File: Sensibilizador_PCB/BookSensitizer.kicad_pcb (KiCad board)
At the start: 2 copper layers, 100 x 100 mm, 37 parts, among them J1 Jack_out, J2 Jack_in, J3 Conn_inputs, M1 Fan, Q1 IRF630, Q2 IRF630, Q3 IRF630, Q4 IRF630, Q5 SI2302, U1 LM5104M, U2 LM5104M

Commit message: Organizado 0 aire
0 aire
ready pa rutear
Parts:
- added REF**: MountingHole_2.5mm, MountingHole:MountingHole_2.5mm, F.Cu at (113.1, 88.9)
- added REF**: MountingHole_2.5mm, MountingHole:MountingHole_2.5mm, F.Cu at (175.0, 123.5)
- added REF**: MountingHole_2.5mm, MountingHole:MountingHole_2.5mm, F.Cu at (113.6, 122.9)
- J1 Vout: renamed from J1
- J2 Vin: renamed from J2
- moved D7 69.9 mm to (166.6, 92.8), turned to -90 degrees
- moved L1 67.8 mm to (136.7, 123.9)
- moved D6 65.5 mm to (121.6, 90.9), turned to 90 degrees
- moved D8 62.5 mm to (166.6, 116.4), turned to 90 degrees
- moved D5 58.8 mm to (121.6, 114.7), turned to 90 degrees
- moved M1 33.2 mm to (176.3, 90.3), turned to 90 degrees
- moved U1 27.4 mm to (119.9, 103.6), turned to 90 degrees
- moved C6 24.9 mm to (167.4, 99.0), turned to 180 degrees
- moved R2 24.6 mm to (119.1, 114.8), turned to -90 degrees
- moved Q5 24.5 mm to (170.4, 86.1), turned to 0 degrees
- moved R7 23.8 mm to (169.1, 116.4), turned to -90 degrees
- moved Q2 23.3 mm to (125.0, 89.3), turned to -90 degrees
- moved D2 22.9 mm to (135.9, 89.3), turned to -90 degrees
- moved J1 Vout 22.7 mm to (164.9, 78.9), turned to 180 degrees
- moved R3 22.0 mm to (120.2, 94.8)
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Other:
- board size 100 x 100 mm -> 70 x 57 mm
- board text added: "+"
- board text added: "-"
- board text added: "Fan"
- board text added: "GND"
- board text added: "PWM1"
- board text added: "PWM2"

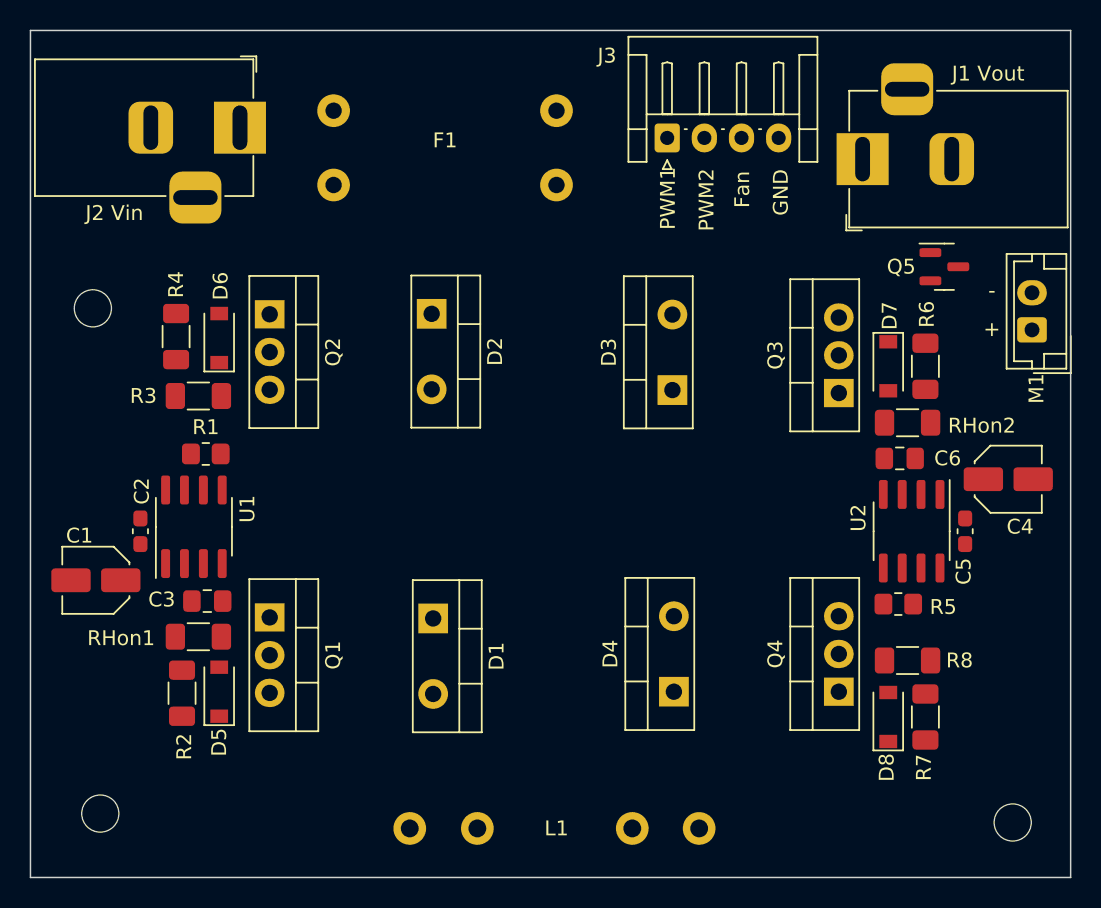
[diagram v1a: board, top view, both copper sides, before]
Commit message: mini cambio en label de RHon
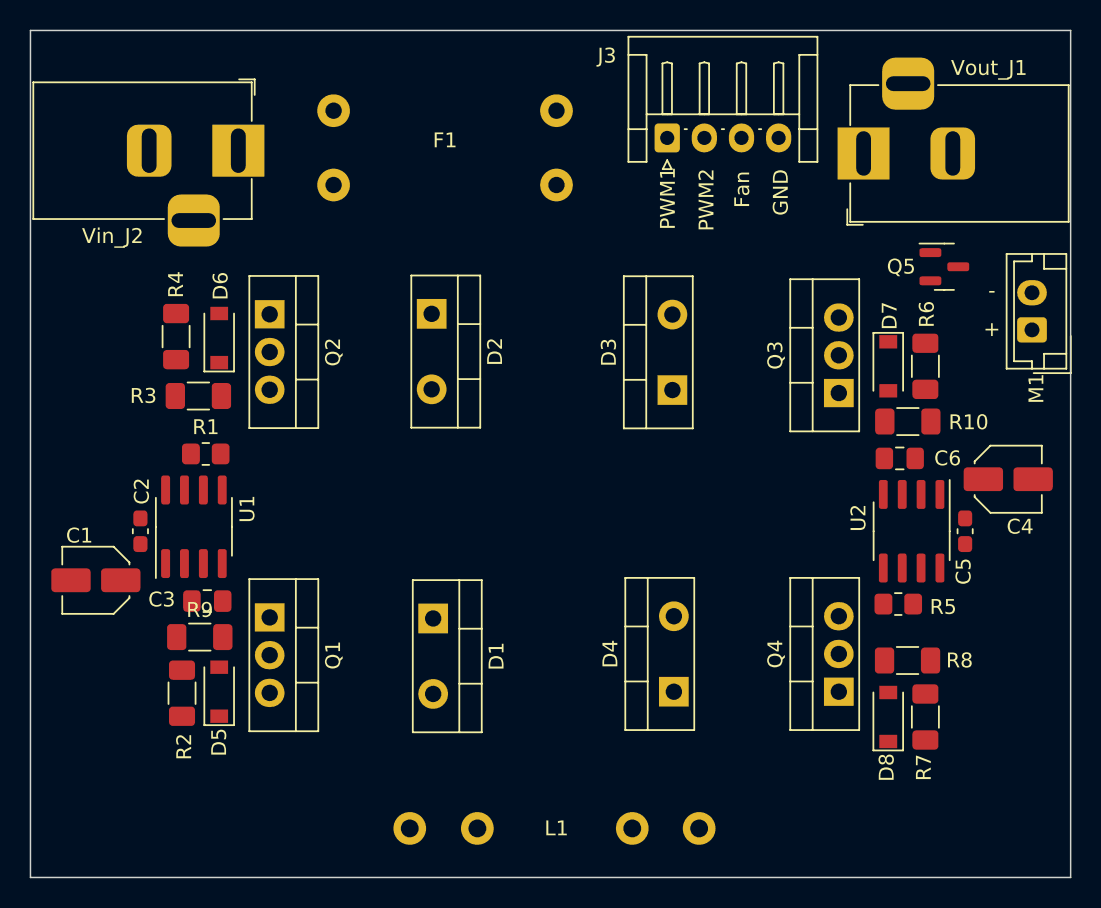
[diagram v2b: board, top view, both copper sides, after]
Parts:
- removed J1 Vout: Jack_out, Connector_BarrelJack:BarrelJack_Horizontal
- removed J2 Vin: Jack_in, Connector_BarrelJack:BarrelJack_Horizontal
- removed REF** (x3): MountingHole_2.5mm, MountingHole:MountingHole_2.5mm
- removed RHon1, RHon2: 2.74 1/4W, Resistor_SMD:R_1206_3216Metric_Pad1.30x1.75mm_HandSolder
- added R10: 2.74 1/4W, Resistor_SMD:R_1206_3216Metric_Pad1.30x1.75mm_HandSolder, F.Cu at (167.9, 96.5)
- added R9: 2.74 1/4W, Resistor_SMD:R_1206_3216Metric_Pad1.30x1.75mm_HandSolder, F.Cu at (120.3, 111.0)
- added Vin_J2: Jack_in, Connector_BarrelJack:BarrelJack_Horizontal, F.Cu at (122.9, 78.3)
- added Vout_J1: Jack_out, Connector_BarrelJack:BarrelJack_Horizontal, F.Cu at (165.0, 78.5)

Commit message: la mitad de los trazos
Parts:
- moved C3 7.00 mm to (124.7, 102.8)
- moved C6 5.71 mm to (163.3, 103.0)
- moved D5 3.63 mm to (121.6, 111.1)
- moved R2 3.63 mm to (119.1, 111.2)
- moved R9 3.63 mm to (120.3, 107.4)
- moved C1 1.57 mm to (113.4, 105.6)
- moved C2 1.57 mm to (116.4, 102.3)
- moved R1 1.57 mm to (120.8, 97.1)
- moved U1 1.57 mm to (120.0, 102.0)
- moved R5 0.55 mm to (167.3, 108.3)
- moved U2 0.47 mm to (168.1, 103.4)
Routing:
- net /in_1: track 0.00 -> 55.5 mm, vias 0 -> 2
- net /in_2: track 0.00 -> 43.6 mm, vias 0 -> 2
- net /in_3: track 0.00 -> 19.1 mm
- net Net-(R7-Pad1): track 0.00 -> 9.33 mm
- net Net-(R6-Pad1): track 0.00 -> 8.34 mm
- net Net-(R3-Pad1): track 0.00 -> 7.40 mm
- net Net-(R2-Pad1): track 0.00 -> 6.60 mm
- net Net-(M1-Pad2): track 0.00 -> 6.35 mm
- net /driver1/G_low: track 0.00 -> 6.32 mm
- net Net-(C6-Pad1): track 0.00 -> 6.24 mm
- net Net-(C3-Pad1): track 0.00 -> 5.75 mm
- net /driver2/Hs: track 0.00 -> 5.73 mm
- net /driver1/G_High: track 0.00 -> 5.62 mm
- net /driver2/G_low: track 0.00 -> 5.60 mm
- net /driver2/G_High: track 0.00 -> 5.55 mm
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- added copper zone on B.Cu, net /driver1/Hs

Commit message: PCB lista
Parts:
- moved Q5 0.87 mm to (171.3, 86.1)
- moved M1 0.19 mm to (176.1, 90.3)
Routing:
- net Net-(F1-Pad1): track 0.00 -> 19.9 mm
- net +12V: track 0.00 -> 6.05 mm
- net GND: track 0.00 -> 5.16 mm
- net Net-(M1-Pad2): track 6.35 -> 5.39 mm
- net /in_3: track 19.1 -> 19.4 mm, vias 0 -> 1
- net /in_1: track 55.5 -> 55.4 mm, vias 2 -> 1
- net /in_2: vias 2 -> 1
- net /driver2/Hs: vias 0 -> 1
- net /driver1/Hs: vias 0 -> 1
- added copper zone on F.Cu, net +12V
- added copper zone on B.Cu, net /driver2/Hs
- added copper zone on F.Cu, net GND

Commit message: Con tornillos
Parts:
- added T1: MountingHole_3.2mm_M3, MountingHole:MountingHole_3.2mm_M3, F.Cu at (115.4, 120.4)
- added T2: MountingHole_3.2mm_M3, MountingHole:MountingHole_3.2mm_M3, F.Cu at (113.9, 87.8)
- added T3: MountingHole_3.2mm_M3, MountingHole:MountingHole_3.2mm_M3, F.Cu at (173.2, 121.9)
- F1 10A: renamed from F1
- moved C2 0.55 mm to (116.4, 101.8)
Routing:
- net +12V: track 6.05 -> 0.03 mm
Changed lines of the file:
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@@
   )
   (footprint "Capacitor_SMD:C_0603_1608Metric_Pad1.08x0.95mm_HandSolder" (layer "F.Cu")
-    (at 116.3714 102.3326 90)
+    (at 116.3828 101.7778 90)
     (descr "Capacitor SMD 0603 (1608 Metric), square (rectangular) end terminal, IPC_7351 nominal with elongated pad for handsoldering. (Body size source: IPC-SM-782 page 76, https://www.pcb-3d.com/wordpress/wp-content/uploads/ipc-sm-782a_amendment_1_and_2.pdf), generated with kicad-footprint-generator")
     (tags "capacitor handsolder")
@@
     (property "Sheetname" "")
     (attr through_hole)
-    (fp_text reference "Vin_J2" (at -8.45 5.75) (layer "F.SilkS")
+    (fp_text reference "Vin_J2" (at -8.5908 -5.6973) (layer "F.SilkS")
       (effects (font (size 1 1) (thickness 0.15)))
     )
@@
     )
   )
+  (footprint "MountingHole:MountingHole_3.2mm_M3" (layer "F.Cu")
+    (at 113.9444 87.8332)
+    (descr "Mounting Hole 3.2mm, no annular, M3")
+    (tags "mounting hole 3.2mm no annular m3")
+    (attr exclude_from_pos_files exclude_from_bom)
+    (fp_text reference "T2" (at 0 -4.2) (layer "User.1")
+      (effects (font (size 1 1) (thickness 0.15)))
+    )
+    (fp_text value "MountingHole_3.2mm_M3" (at 0 4.2) (layer "F.Fab")
+      (effects (font (size 1 1) (thickness 0.15)))
+    )
+    (fp_text user "${REFERENCE}" (at 0 0) (layer "F.Fab")
+      (effects (font (size 1 1) (thickness 0.15)))
+    )
+    (fp_circle (center 0 0) (end 3.2 0) (layer "Cmts.User") (width 0.15) (fill none))
+    (fp_circle (center 0 0) (end 3.45 0) (layer "F.CrtYd") (width 0.05) (fill none))
+    (pad "" np_thru_hole circle (at 0 0) (size 3.2 3.2) (drill 3.2) (layers *.Cu *.Mask))
+  )
   (footprint "Resistor_SMD:R_1206_3216Metric_Pad1.30x1.75mm_HandSolder" (layer "F.Cu")
     (at 120.3198 107.3912)
@@
     )
   )
+  (footprint "MountingHole:MountingHole_3.2mm_M3" (layer "F.Cu")
+    (at 173.228 121.8692)
+    (descr "Mounting Hole 3.2mm, no annular, M3")
+    (tags "mounting hole 3.2mm no annular m3")
+    (attr exclude_from_pos_files exclude_from_bom)
+    (fp_text reference "T3" (at 0 -4.2) (layer "User.1")
+      (effects (font (size 1 1) (thickness 0.15)))
+    )
+    (fp_text value "MountingHole_3.2mm_M3" (at 0 4.2) (layer "F.Fab")
+      (effects (font (size 1 1) (thickness 0.15)))
+    )
+    (fp_text user "${REFERENCE}" (at 0 0) (layer "F.Fab")
+      (effects (font (size 1 1) (thickness 0.15)))
+    )
+    (fp_circle (center 0 0) (end 3.2 0) (layer "Cmts.User") (width 0.15) (fill none))
+    (fp_circle (center 0 0) (end 3.45 0) (layer "F.CrtYd") (width 0.05) (fill none))
+    (pad "" np_thru_hole circle (at 0 0) (size 3.2 3.2) (drill 3.2) (layers *.Cu *.Mask))
+  )
   (footprint "Resistor_SMD:R_1206_3216Metric_Pad1.30x1.75mm_HandSolder" (layer "F.Cu")
     (at 167.9448 96.52 180)
@@
     (property "Sheetname" "")
     (attr through_hole)
-    (fp_text reference "F1" (at 0 -0.5 unlocked) (layer "F.SilkS")
+    (fp_text reference "F1 10A" (at -4.3644 -4.7956 unlocked) (layer "F.SilkS")
       (effects (font (size 1 1) (thickness 0.15)))
     )
@@
     (pad "2" thru_hole circle (at 17.2 0) (size 2.2 2.2) (drill 1.2) (layers *.Cu *.Mask)
       (net 6 "/driver2/Hs") (pinfunction "2") (pintype "passive"))
+  )
+  (footprint "MountingHole:MountingHole_3.2mm_M3" (layer "F.Cu")
+    (at 115.3922 120.4468)
+    (descr "Mounting Hole 3.2mm, no annular, M3")
+    (tags "mounting hole 3.2mm no annular m3")
+    (attr exclude_from_pos_files exclude_from_bom)
+    (fp_text reference "T1" (at 0 -4.2) (layer "User.1")
+      (effects (font (size 1 1) (thickness 0.15)))
+    )
+    (fp_text value "MountingHole_3.2mm_M3" (at 0 4.2) (layer "F.Fab")
+      (effects (font (size 1 1) (thickness 0.15)))
+    )
+    (fp_text user "${REFERENCE}" (at 0 0) (layer "F.Fab")
+      (effects (font (size 1 1) (thickness 0.15)))
+    )
+    (fp_circle (center 0 0) (end 3.2 0) (layer "Cmts.User") (width 0.15) (fill none))
+    (fp_circle (center 0 0) (end 3.45 0) (layer "F.CrtYd") (width 0.05) (fill none))
+    (pad "" np_thru_hole circle (at 0 0) (size 3.2 3.2) (drill 3.2) (layers *.Cu *.Mask))
   )
   (footprint "Diode_SMD:D_SOD-123" (layer "F.Cu")
@@
     (effects (font (size 1 1) (thickness 0.15)))
   )
-  (segment (start 117.7551 103.1951) (end 118.0664 103.5064) (width 0.7) (layer "F.Cu") (net 1))
   (segment (start 176.3 90.35) (end 176.28 90.33) (width 1) (layer "F.Cu") (net 1))
-  (segment (start 172.4712 100.9538) (end 173.025 100.4) (width 0.7) (layer "F.Cu") (net 1))
-  (segment (start 118.0664 103.5064) (end 118.0664 104.5076) (width 0.7) (layer "F.Cu") (net 1))
-  (segment (start 170.053 100.9538) (end 172.4712 100.9538) (width 0.7) (layer "F.Cu") (net 1))
-  (segment (start 116.3714 103.1951) (end 117.7551 103.1951) (width 0.7) (layer "F.Cu") (net 1))
   (segment (start 168.783 107.7718) (end 168.3 108.2548) (width 0.7) (layer "F.Cu") (net 2))
   (segment (start 119.3364 99.5576) (end 119.3364 97.5676) (width 0.7) (layer "F.Cu") (net 2))
@@
         (xy 162.23 76.22)
         (xy 167.61 76.15)
-        (xy 167.61 88.05)
-        (xy 173.07 87.98)
-        (xy 173.12 89.09)
-        (xy 177.96 89.09)
+        (xy 167.64 83.312)
+        (xy 173.1518 83.312)
+        (xy 173.156354 83.295057)
+        (xy 177.964554 83.307257)
         (xy 177.92 92.22)
         (xy 174.8 92.22)
         (xy 174.72 103.9)
-        (xy 170.85 103.95)
-        (xy 170.75 89.28)
-        (xy 165.28 89.24)
-        (xy 165.28 93.3)
-        (xy 157.49 93.3)
+        (xy 165.1508 103.886)
+        (xy 165.18692 99.698923)
+        (xy 165.20538 99.44431)
+        (xy 165.227 97.9736)
+        (xy 157.49 97.9736)
         (xy 157.49 98)
         (xy 147.06 98.01)
@@
         (xy 113.44 102.37)
         (xy 117.46 102.37)
-        (xy 117.46 115.68)
-        (xy 123.27 115.68)
-        (xy 123.27 110.98)
-        (xy 129.66 110.98)
-        (xy 129.68 103.22)
-        (xy 141.77 103.22)
+        (xy 117.46 102.3704)
+        (xy 123.27 102.3704)
+        (xy 123.27 102.3694)
+        (xy 129.66 102.3694)
+        (xy 129.68 102.3564)
+        (xy 141.77 102.3564)
         (xy 141.700186 73.240001)
         (xy 141.7 73.21)
